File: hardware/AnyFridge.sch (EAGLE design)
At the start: 7 parts

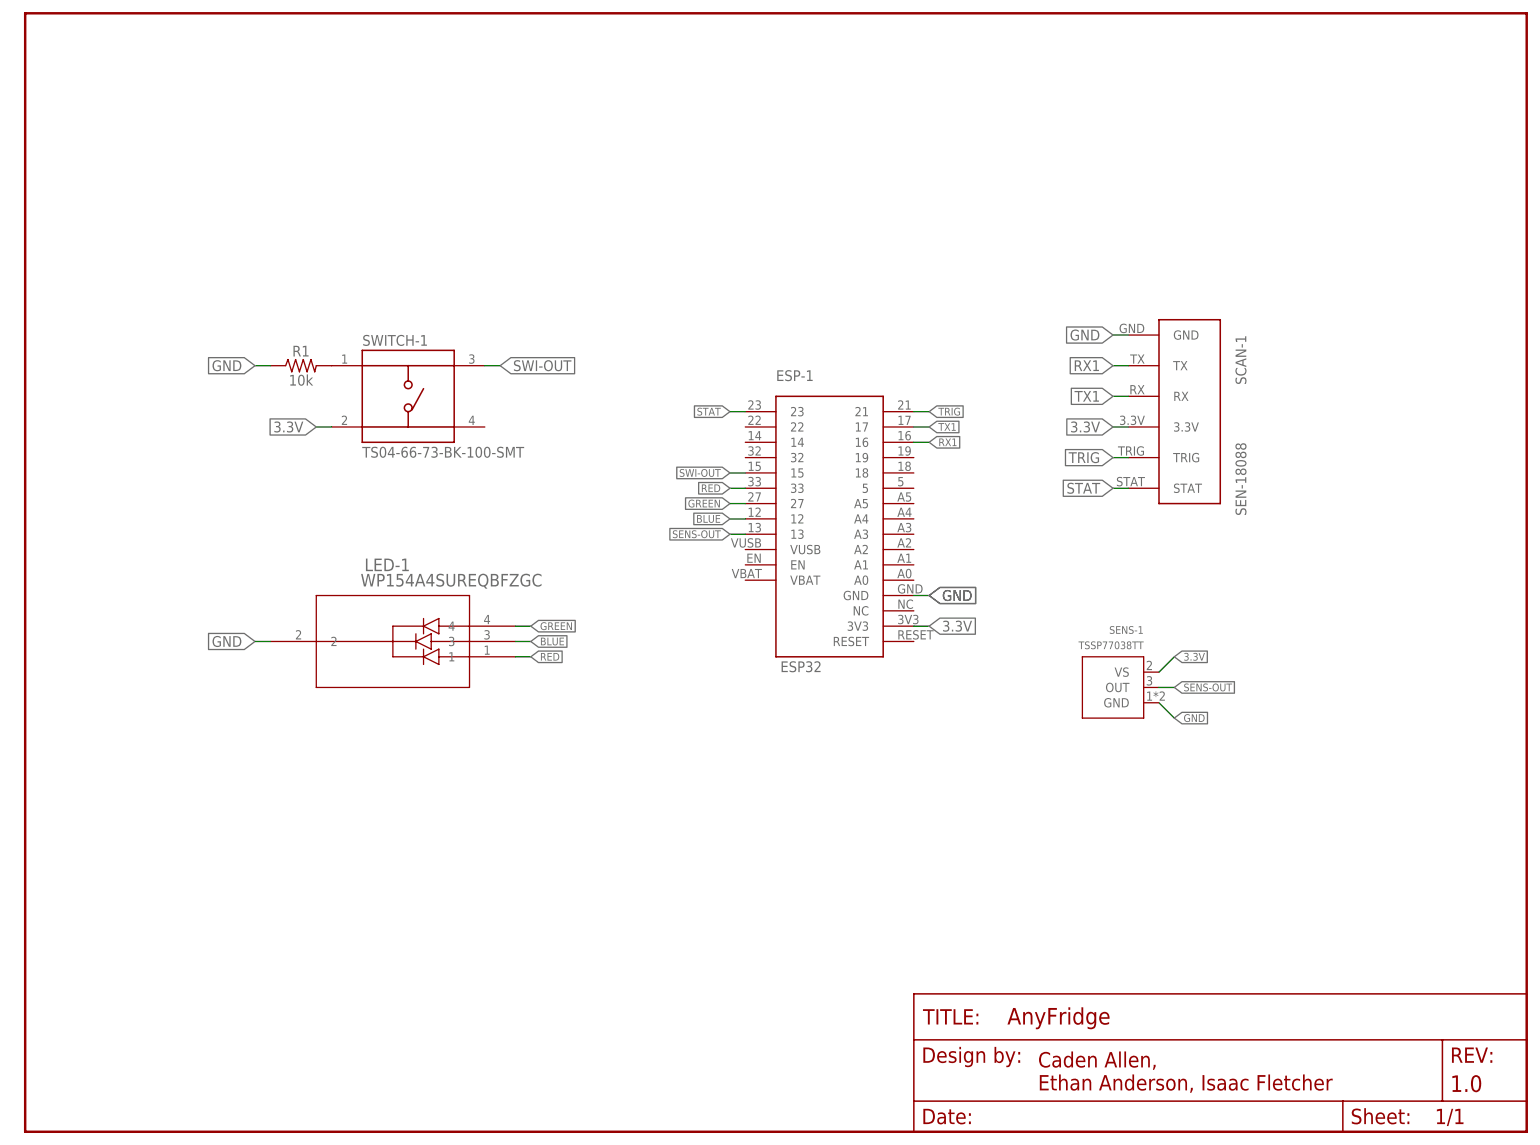
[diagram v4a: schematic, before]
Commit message: Added comment to schematic
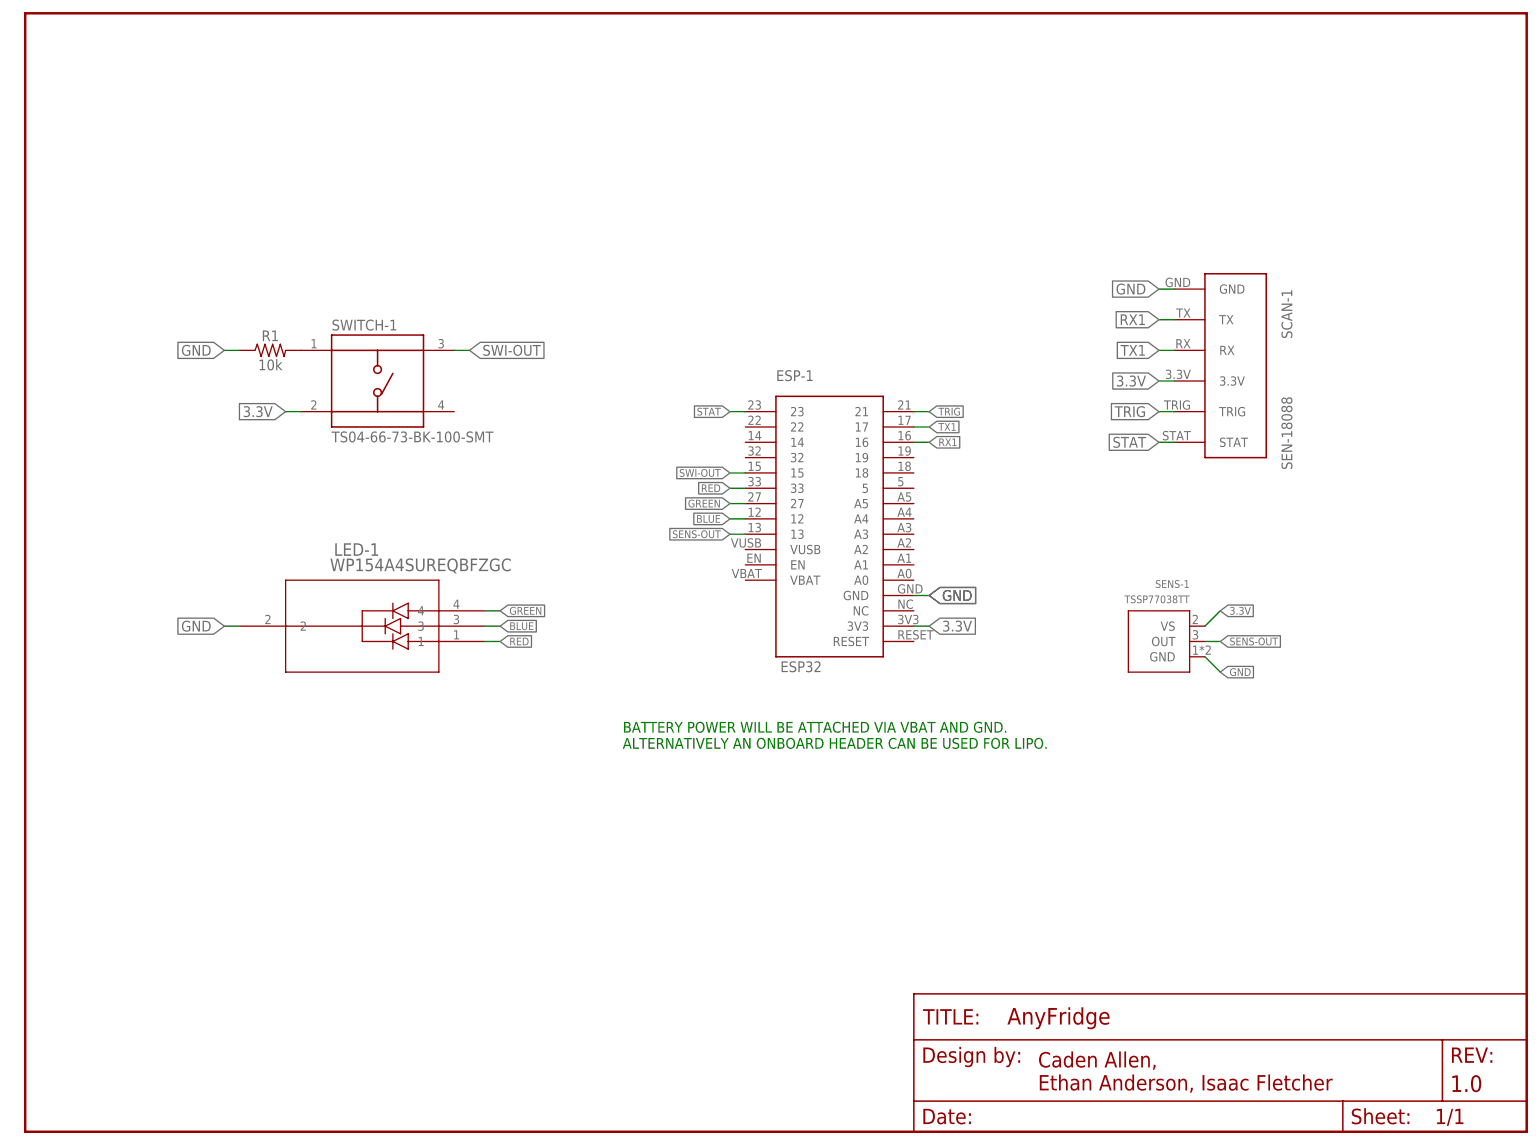
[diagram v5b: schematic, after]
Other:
- note added: "BATTERY POWER WILL BE ATTACHED VIA VBAT AND GND. ALTERNATIVELY AN ONBOARD HEADER CAN BE USED FOR LIPO."
- moved on the sheet: LED-1, R1, SCAN-1, SENS-1, SWITCH-1

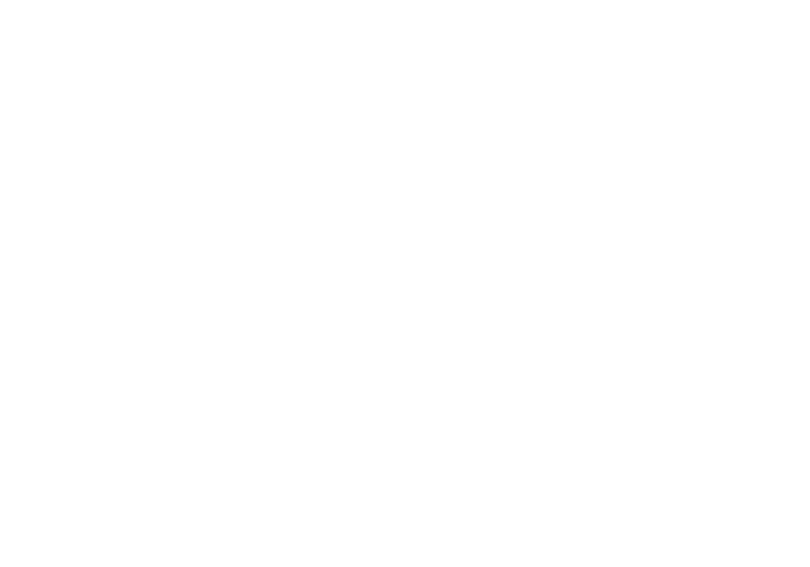
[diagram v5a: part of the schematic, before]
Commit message: Increase traces to 16mm and add test points for UART
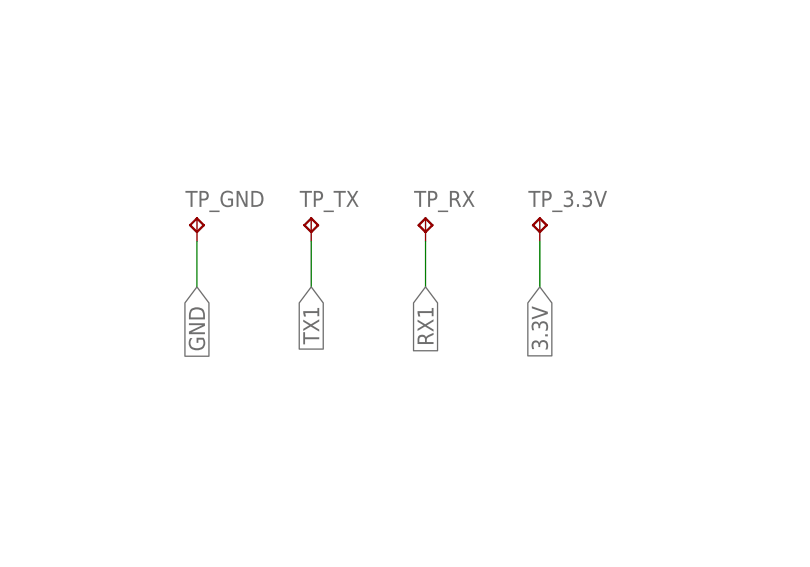
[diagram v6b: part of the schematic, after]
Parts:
- added TP_3.3V, TP_GND, TP_RX, TP_TX: TPPAD1-13, testpad:TPPAD1-13
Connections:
- net 3.3V: now also TP_3.3V.TP
- net GND: now also TP_GND.TP
- net RX1: now also TP_RX.TP
- net TX1: now also TP_TX.TP
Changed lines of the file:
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@@
 <part name="ESP-1" library="ESP32" deviceset="ESP32" device=""/>
 <part name="R1" library="SparkFun-Resistors" library_urn="urn:adsk.eagle:library:532" deviceset="10KOHM" device="-HORIZ-1/4W-1%" package3d_urn="urn:adsk.eagle:package:39658/2" value="10k"/>
+<part name="TP_GND" library="testpad" library_urn="urn:adsk.eagle:library:385" deviceset="TP" device="PAD1-13" package3d_urn="urn:adsk.eagle:package:27946/1"/>
+<part name="TP_TX" library="testpad" library_urn="urn:adsk.eagle:library:385" deviceset="TP" device="PAD1-13" package3d_urn="urn:adsk.eagle:package:27946/1"/>
+<part name="TP_RX" library="testpad" library_urn="urn:adsk.eagle:library:385" deviceset="TP" device="PAD1-13" package3d_urn="urn:adsk.eagle:package:27946/1"/>
+<part name="TP_3.3V" library="testpad" library_urn="urn:adsk.eagle:library:385" deviceset="TP" device="PAD1-13" package3d_urn="urn:adsk.eagle:package:27946/1"/>
 </parts>
 <sheets>
@@
 <attribute name="VALUE" x="40.64" y="128.016" size="1.778" layer="96" font="vector" align="top-center"/>
 </instance>
+<instance part="TP_GND" gate="G$1" x="27.94" y="43.18" smashed="yes">
+<attribute name="NAME" x="26.67" y="44.45" size="1.778" layer="95"/>
+<attribute name="TP_SIGNAL_NAME" x="29.21" y="41.91" size="1.778" layer="97"/>
+</instance>
+<instance part="TP_TX" gate="G$1" x="40.64" y="43.18" smashed="yes">
+<attribute name="NAME" x="39.37" y="44.45" size="1.778" layer="95"/>
+<attribute name="TP_SIGNAL_NAME" x="41.91" y="41.91" size="1.778" layer="97"/>
+</instance>
+<instance part="TP_RX" gate="G$1" x="53.34" y="43.18" smashed="yes">
+<attribute name="NAME" x="52.07" y="44.45" size="1.778" layer="95"/>
+<attribute name="TP_SIGNAL_NAME" x="54.61" y="41.91" size="1.778" layer="97"/>
+</instance>
+<instance part="TP_3.3V" gate="G$1" x="66.04" y="43.18" smashed="yes">
+<attribute name="NAME" x="64.77" y="44.45" size="1.778" layer="95"/>
+<attribute name="TP_SIGNAL_NAME" x="67.31" y="41.91" size="1.778" layer="97"/>
+</instance>
 </instances>
 <busses>
@@
 <label x="33.02" y="129.54" size="1.778" layer="95" rot="R180" xref="yes" grouprefs="SWITCH"/>
 </segment>
+<segment>
+<pinref part="TP_GND" gate="G$1" pin="TP"/>
+<wire x1="27.94" y1="40.64" x2="27.94" y2="35.56" width="0.1524" layer="91"/>
+<label x="27.94" y="35.56" size="1.778" layer="95" rot="R270" xref="yes"/>
+</segment>
 </net>
 <net name="3.3V" class="0">
@@
 <label x="43.18" y="119.38" size="1.778" layer="95" rot="R180" xref="yes" grouprefs="SWITCH"/>
 </segment>
+<segment>
+<pinref part="TP_3.3V" gate="G$1" pin="TP"/>
+<wire x1="66.04" y1="40.64" x2="66.04" y2="35.56" width="0.1524" layer="91"/>
+<label x="66.04" y="35.56" size="1.778" layer="95" rot="R270" xref="yes"/>
+</segment>
 </net>
 <net name="TRIG" class="0">
@@
 <label x="187.96" y="129.54" size="1.778" layer="95" rot="R180" xref="yes" grouprefs="SCANNER"/>
 </segment>
+<segment>
+<pinref part="TP_TX" gate="G$1" pin="TP"/>
+<wire x1="40.64" y1="40.64" x2="40.64" y2="35.56" width="0.1524" layer="91"/>
+<label x="40.64" y="35.56" size="1.778" layer="95" rot="R270" xref="yes"/>
+</segment>
 </net>
 <net name="RX1" class="0">
@@
 <label x="187.96" y="134.62" size="1.778" layer="95" rot="R180" xref="yes" grouprefs="SCANNER"/>
 </segment>
-</net>
+<segment>
+<pinref part="TP_RX" gate="G$1" pin="TP"/>
+<wire x1="53.34" y1="40.64" x2="53.34" y2="35.56" width="0.1524" layer="91"/>
+<label x="53.34" y="35.56" size="1.778" layer="95" rot="R270" xref="yes"/>
+</segment>
+</net>
